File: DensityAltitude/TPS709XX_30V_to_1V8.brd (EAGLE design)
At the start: 63.5 x 57.1 mm, 15 parts, among them U1 V_REG_LD1086V

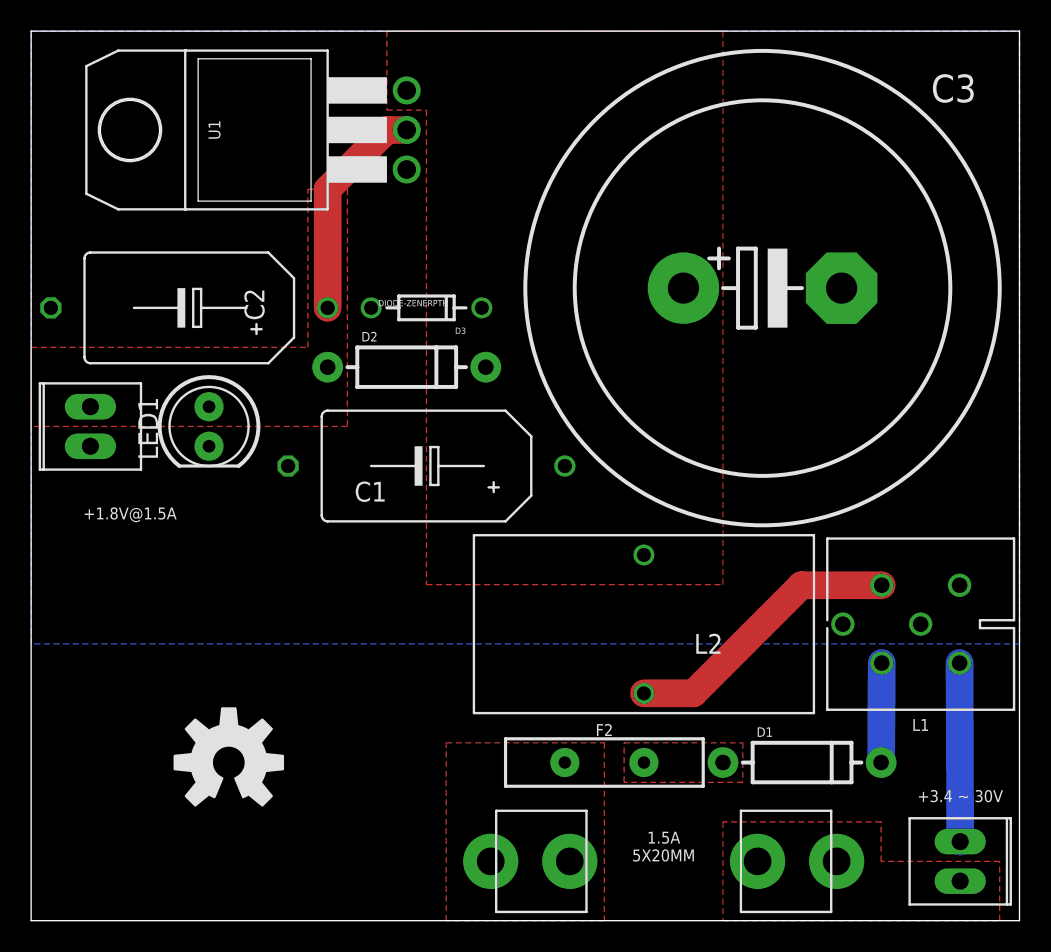
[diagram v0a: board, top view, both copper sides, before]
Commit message: Moved 1V8 voltage regulators from DensityAltitude.lbr to 1V8.lbr More layout work for various high input voltage regulators A bit more work on LowduinoPTH_v2
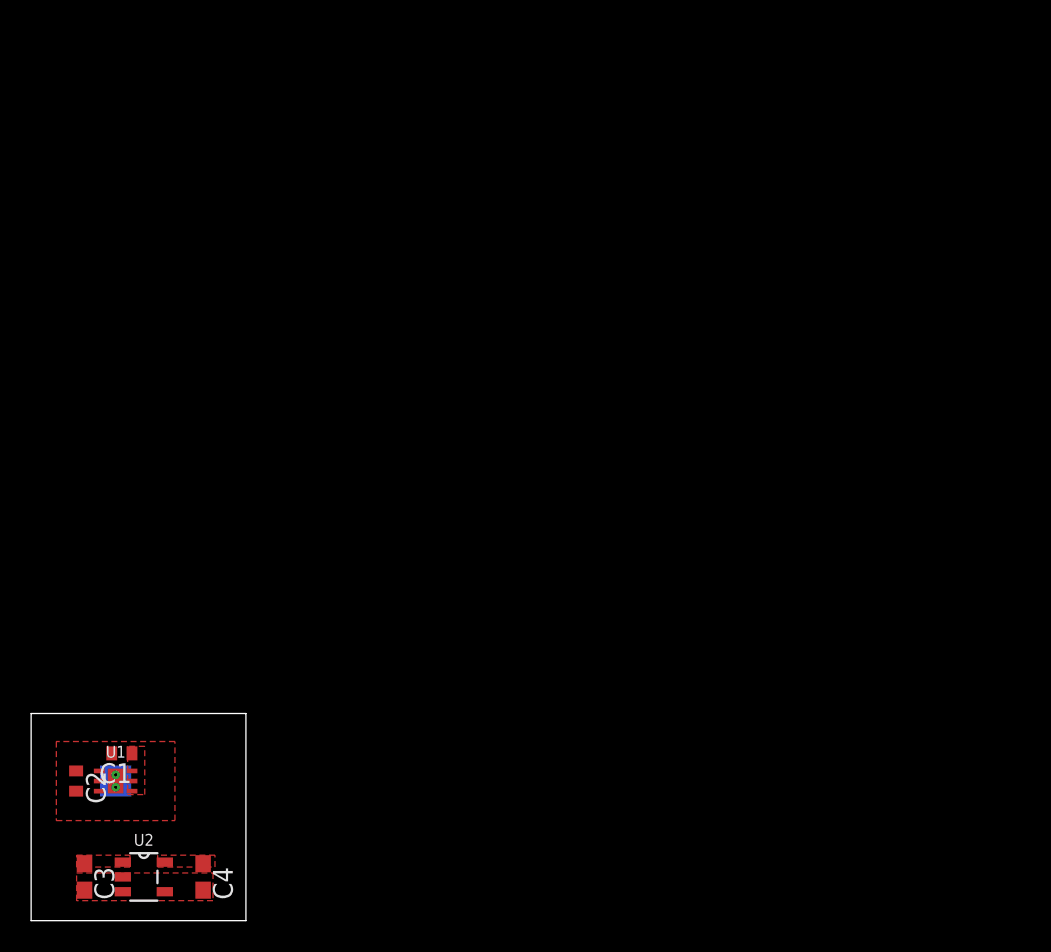
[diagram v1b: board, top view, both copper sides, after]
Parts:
- removed D1, D2: (no value), SparkFun-DiscreteSemi:DIODE-1N4001
- removed D3: DIODE-ZENERPTH, SparkFun-DiscreteSemi:DIODE-ZENER
- removed F1: FUSE5X20MM, DensityAltitude:FUSE_1A3399
- removed F2: PTCPTH, DensityAltitude:PTC
- removed JP1, JP2: (no value), DensityAltitude:1X02_282834-2
- removed L1: BNX002, 1V8:BNX002
- removed L2: 2121-RC-VERT, DensityAltitude:2121-RC-VERT
- removed LED1: (no value), SparkFun-LED:LED5MM
- removed U$2: (no value), SparkFun-Aesthetics:OSHW-LOGO-L
- added C4: (no value), rcl:C0603
- added U2: TPS709DBV, 1V8:DBV
- C1, C2: value 10uF -> (none); device 1V8:KEMET_E -> rcl:C0402
- C3: device rcl:EB30D -> rcl:C0603
- U1: value V_REG_LD1086V -> TPS709DRV; device DensityAltitude:TO-220-SINGLE -> 1V8:DRV
- moved C3 57.7 mm to (3.43, 2.81), turned to 270 degrees
- moved U1 41.8 mm to (5.43, 8.97), turned to 0 degrees
- moved C2 31.3 mm to (2.89, 8.97), turned to 270 degrees
- moved C1 26.9 mm to (5.83, 10.7)
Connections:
- removed net DIODE1: D1.C, L1.B
- removed net FILTERED: C1.+, C3.+, D2.C, D3.P$1, L2.2, U1.IN
- removed net FUSE1: F1.3, F1.4, F2.P$1
- removed net FUSE2: D1.A, F2.P$2
- removed net GND-ISO: C1.-, C2.-, C3.-, D3.P$2, JP2.P$1, L1.CG, L1.CG1, L1.CG2, LED1.K, U1.GND
- removed net N$1: L1.CB, L2.1
- removed net VCC: C2.+, D2.A, JP2.P$2, LED1.A, U1.OUT
- new net VOUT1: C2.1, U1.1
- new net VOUT2: C4.1, U2.5
- net GND: now also C1.2, C2.2, C3.2, C4.2, U1.3, U1.7, U1.8, U1.V1, U1.V2, U2.2; no longer JP1.P$1, L1.PSG
- net VIN: now also C1.1, C3.1, U1.4, U1.6, U2.1, U2.3; no longer F1.1, F1.2, JP1.P$2
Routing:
- net N$1: track 18.2 -> 0.00 mm
- net VCC: track 14.3 -> 0.00 mm
- net GND: track 11.5 -> 0.00 mm
- net DIODE1: track 6.39 -> 0.00 mm
- added copper zone on layer 1, net GND
- added copper zone on layer 1, net VOUT2
- removed copper zone on layer 1, net FILTERED
- removed copper zone on layer 1, net FUSE1
- removed copper zone on layer 1, net FUSE2
- removed copper zone on layer 16, net GND-ISO
- removed copper zone on layer 1, net VCC
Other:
- board size 63.5 x 57.1 mm -> 13.8 x 13.3 mm
- board text removed: "+1.8V@1.5A"
- board text removed: "+3.4 ~ 30V"
- board text removed: "1.5A 5X20MM"
